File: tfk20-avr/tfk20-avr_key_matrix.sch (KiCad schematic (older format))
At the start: 48 parts

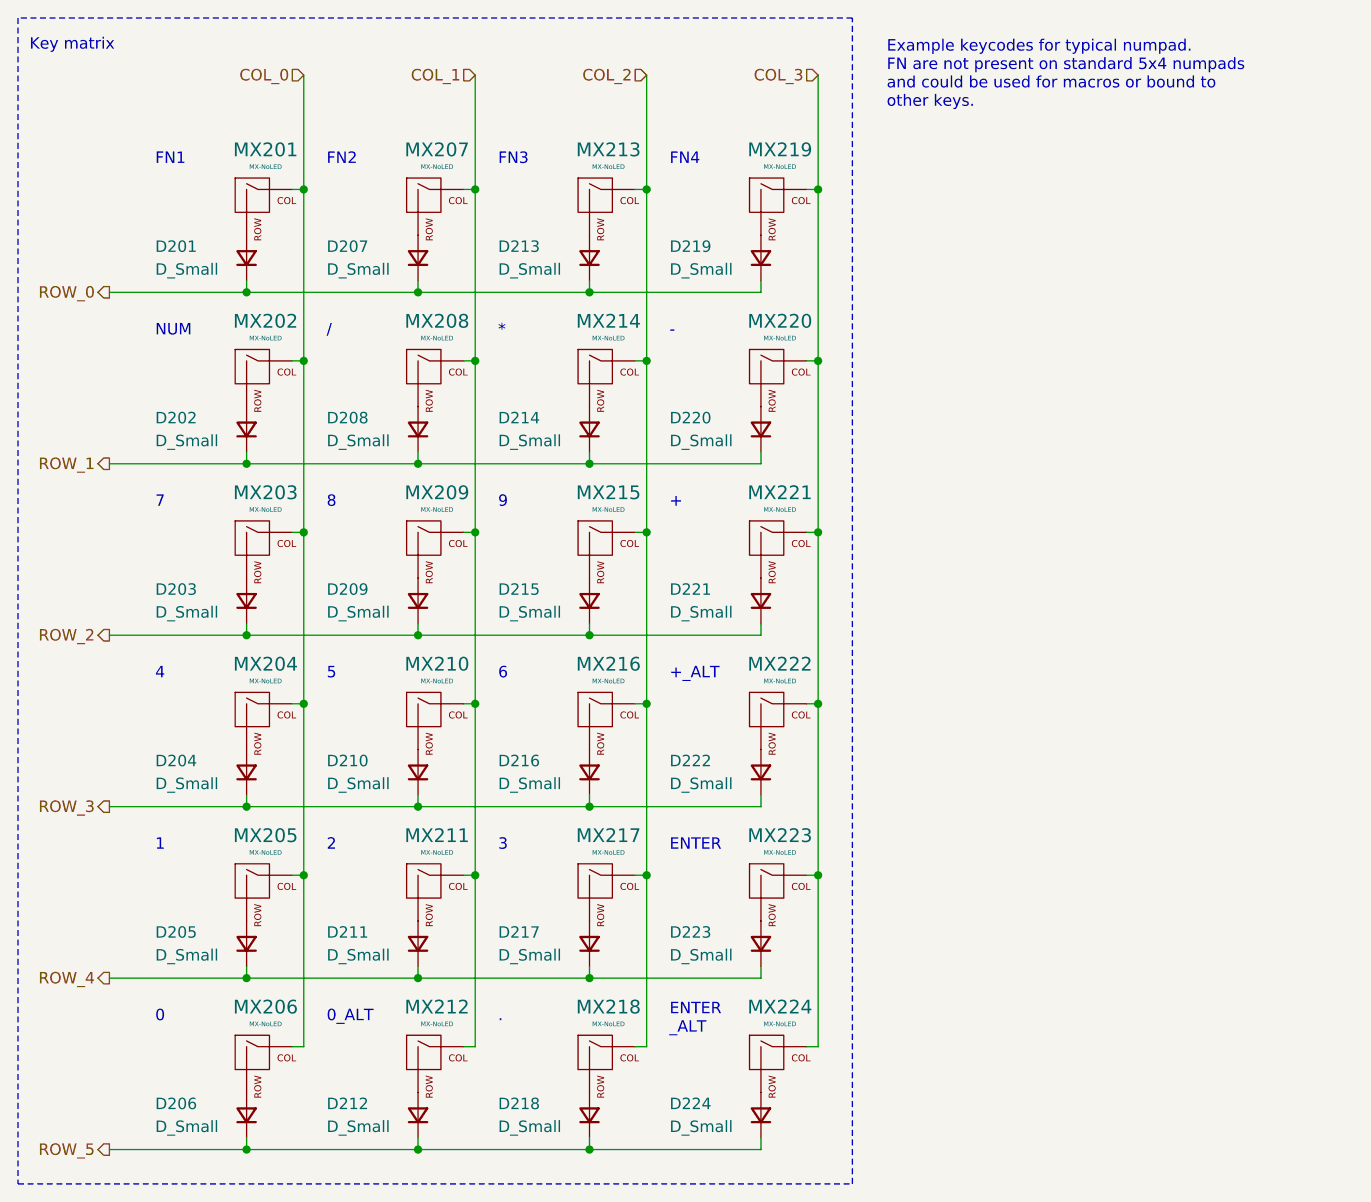
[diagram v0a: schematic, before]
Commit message: Add mounting holes
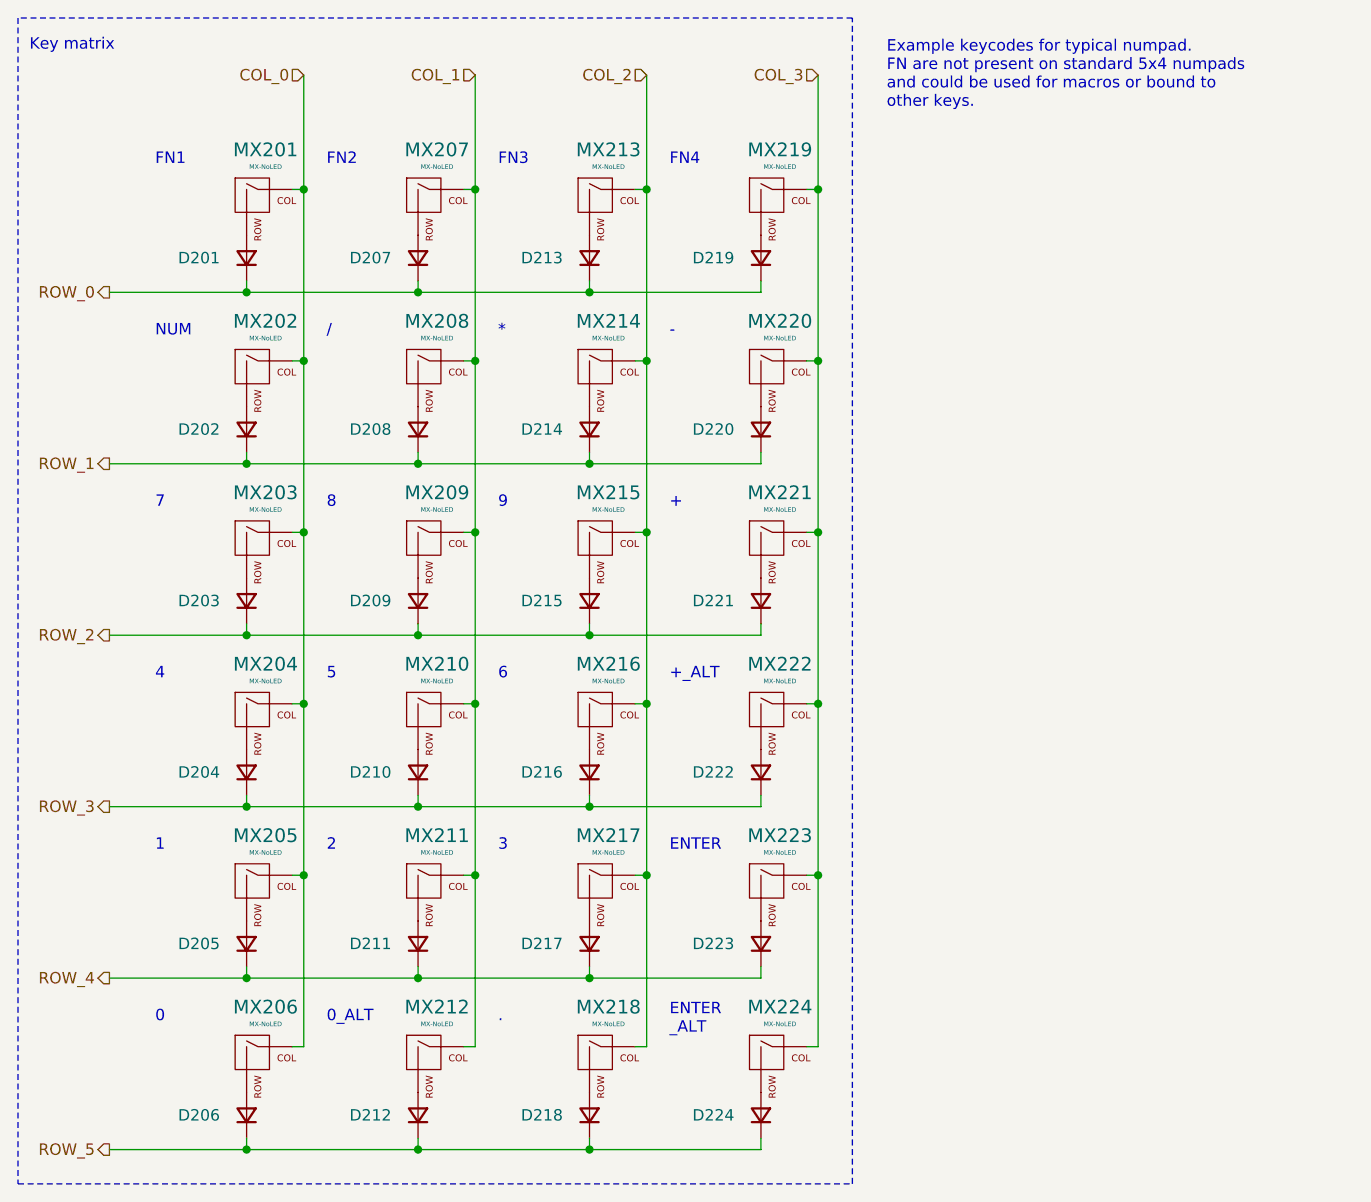
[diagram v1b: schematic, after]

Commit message: Remove alternative switch positions
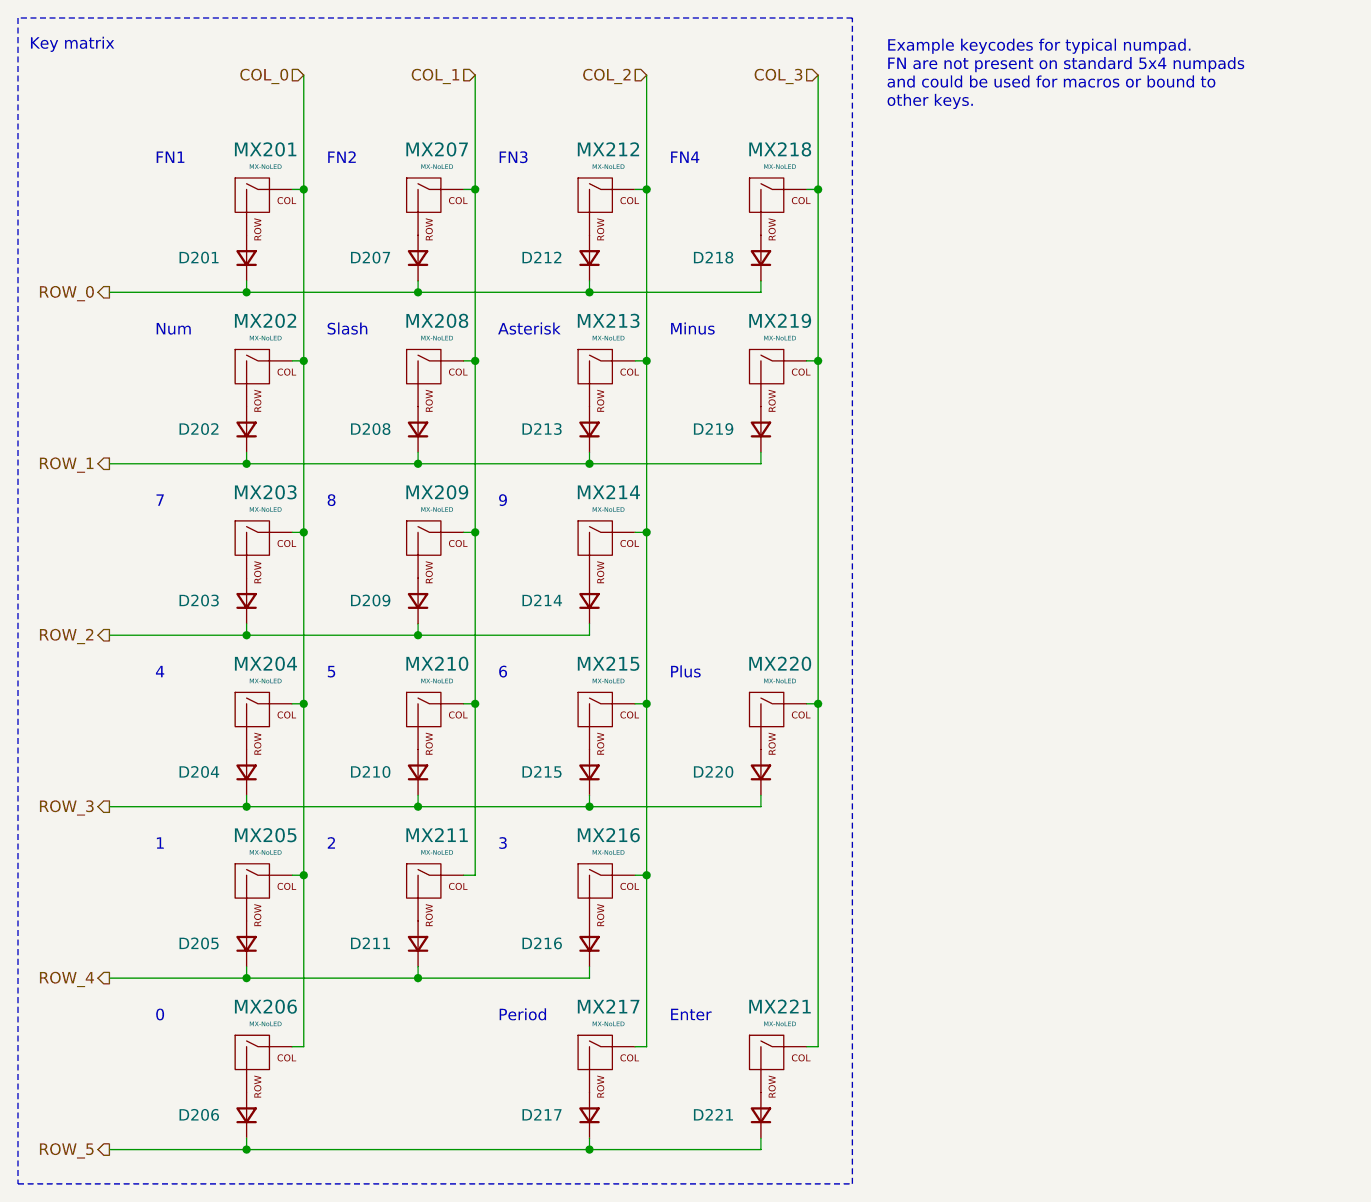
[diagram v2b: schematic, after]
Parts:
- removed D212, D221, D223: D_Small, symbol Device:D_Small
- removed MX212, MX221, MX223: MX-NoLED, symbol MX_Alps_Hybrid:MX-NoLED
- renumbered D213 to D212, D214 to D213, D215 to D214, D216 to D215, D217 to D216, D218 to D217, D219 to D218, D220 to D219, D222 to D220, D224 to D221, MX213 to MX212, MX214 to MX213, MX215 to MX214, MX216 to MX215, MX217 to MX216, MX218 to MX217, MX219 to MX218, MX220 to MX219, MX222 to MX220, MX224 to MX221
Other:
- note added: "Asterisk"
- note added: "Enter"
- note added: "Minus"
- note added: "Num"
- note added: "Period"
- note added: "Plus"
- note added: "Slash"
- note removed: "*"
- note removed: "+"
- note removed: "+_ALT"
- note removed: "-"
- note removed: "."
- note removed: "/"
- note removed: "0_ALT"
- note removed: "ENTER"
- note removed: "ENTER\n_ALT"
- note removed: "NUM\n"
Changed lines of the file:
@@
 $EndComp
 $Comp
-L MX_Alps_Hybrid:MX-NoLED MX214
+L MX_Alps_Hybrid:MX-NoLED MX213
 U 1 1 60307FEB
 P 6150 2550
-F 0 "MX214" H 6183 2773 60  0000 C CNN
+F 0 "MX213" H 6183 2773 60  0000 C CNN
 F 1 "MX-NoLED" H 6183 2699 20  0000 C CNN
 F 2 "" H 5525 2525 60  0001 C CNN
@@
 $EndComp
 $Comp
-L MX_Alps_Hybrid:MX-NoLED MX215
+L MX_Alps_Hybrid:MX-NoLED MX214
 U 1 1 60307FF7
 P 6150 3300
-F 0 "MX215" H 6183 3523 60  0000 C CNN
+F 0 "MX214" H 6183 3523 60  0000 C CNN
 F 1 "MX-NoLED" H 6183 3449 20  0000 C CNN
 F 2 "" H 5525 3275 60  0001 C CNN
@@
 $EndComp
 $Comp
-L MX_Alps_Hybrid:MX-NoLED MX220
+L MX_Alps_Hybrid:MX-NoLED MX219
 U 1 1 60307FFD
 P 6900 2550
-F 0 "MX220" H 6933 2773 60  0000 C CNN
+F 0 "MX219" H 6933 2773 60  0000 C CNN
 F 1 "MX-NoLED" H 6933 2699 20  0000 C CNN
 F 2 "" H 6275 2525 60  0001 C CNN
 F 3 "" H 6275 2525 60  0001 C CNN
 	1    6900 2550
-	1    0    0    -1
-$EndComp
-$Comp
-L MX_Alps_Hybrid:MX-NoLED MX221
-U 1 1 60308003
-P 6900 3300
-F 0 "MX221" H 6933 3523 60  0000 C CNN
-F 1 "MX-NoLED" H 6933 3449 20  0000 C CNN
-F 2 "" H 6275 3275 60  0001 C CNN
-F 3 "" H 6275 3275 60  0001 C CNN
-	1    6900 3300
 	1    0    0    -1
 $EndComp
@@
 $EndComp
 $Comp
-L MX_Alps_Hybrid:MX-NoLED MX216
+L MX_Alps_Hybrid:MX-NoLED MX215
 U 1 1 60314CE4
 P 6150 4050
-F 0 "MX216" H 6183 4273 60  0000 C CNN
+F 0 "MX215" H 6183 4273 60  0000 C CNN
 F 1 "MX-NoLED" H 6183 4199 20  0000 C CNN
 F 2 "" H 5525 4025 60  0001 C CNN
@@
 $EndComp
 $Comp
-L MX_Alps_Hybrid:MX-NoLED MX222
+L MX_Alps_Hybrid:MX-NoLED MX220
 U 1 1 60314CEA
 P 6900 4050
-F 0 "MX222" H 6933 4273 60  0000 C CNN
+F 0 "MX220" H 6933 4273 60  0000 C CNN
 F 1 "MX-NoLED" H 6933 4199 20  0000 C CNN
 F 2 "" H 6275 4025 60  0001 C CNN
@@
 $EndComp
 $Comp
-L MX_Alps_Hybrid:MX-NoLED MX217
+L MX_Alps_Hybrid:MX-NoLED MX216
 U 1 1 6031D490
 P 6150 4800
-F 0 "MX217" H 6183 5023 60  0000 C CNN
+F 0 "MX216" H 6183 5023 60  0000 C CNN
 F 1 "MX-NoLED" H 6183 4949 20  0000 C CNN
 F 2 "" H 5525 4775 60  0001 C CNN
 F 3 "" H 5525 4775 60  0001 C CNN
 	1    6150 4800
-	1    0    0    -1
-$EndComp
-$Comp
-L MX_Alps_Hybrid:MX-NoLED MX223
-U 1 1 6031D496
-P 6900 4800
-F 0 "MX223" H 6933 5023 60  0000 C CNN
-F 1 "MX-NoLED" H 6933 4949 20  0000 C CNN
-F 2 "" H 6275 4775 60  0001 C CNN
-F 3 "" H 6275 4775 60  0001 C CNN
-	1    6900 4800
 	1    0    0    -1
 $EndComp
@@
 $EndComp
 $Comp
-L MX_Alps_Hybrid:MX-NoLED MX212
-U 1 1 6032525B
-P 5400 5550
-F 0 "MX212" H 5433 5773 60  0000 C CNN
-F 1 "MX-NoLED" H 5433 5699 20  0000 C CNN
-F 2 "" H 4775 5525 60  0001 C CNN
-F 3 "" H 4775 5525 60  0001 C CNN
-	1    5400 5550
-	1    0    0    -1
-$EndComp
-$Comp
-L MX_Alps_Hybrid:MX-NoLED MX218
+L MX_Alps_Hybrid:MX-NoLED MX217
 U 1 1 6032526D
 P 6150 5550
-F 0 "MX218" H 6183 5773 60  0000 C CNN
+F 0 "MX217" H 6183 5773 60  0000 C CNN
 F 1 "MX-NoLED" H 6183 5699 20  0000 C CNN
 F 2 "" H 5525 5525 60  0001 C CNN
@@
 $EndComp
 $Comp
-L MX_Alps_Hybrid:MX-NoLED MX224
+L MX_Alps_Hybrid:MX-NoLED MX221
 U 1 1 60325273
 P 6900 5550
-F 0 "MX224" H 6933 5773 60  0000 C CNN
+F 0 "MX221" H 6933 5773 60  0000 C CNN
 F 1 "MX-NoLED" H 6933 5699 20  0000 C CNN
 F 2 "" H 6275 5525 60  0001 C CNN
@@
 	4850 5500 4800 5500
 Wire Wire Line
-	5600 5500 5550 5500
-Wire Wire Line
 	6350 5500 6300 5500
 Wire Wire Line
@@
 Wire Wire Line
 	5550 4750 5600 4750
-Connection ~ 5600 4750
-Wire Wire Line
-	5600 4750 5600 5500
 Wire Wire Line
 	6300 2500 6350 2500
@@
 	6350 4750 6350 5500
 Wire Wire Line
-	7050 4750 7100 4750
-Connection ~ 7100 4750
-Wire Wire Line
-	7100 4750 7100 5500
-Wire Wire Line
 	7050 4000 7100 4000
 Connection ~ 7100 4000
 Wire Wire Line
-	7100 4000 7100 4750
-Wire Wire Line
-	7050 3250 7100 3250
-Connection ~ 7100 3250
-Wire Wire Line
-	7100 3250 7100 4000
-Wire Wire Line
 	7050 2500 7100 2500
 Connection ~ 7100 2500
@@
 	4000 3700 4600 3700
 Wire Wire Line
-	6850 3700 6850 3650
-Wire Wire Line
 	6100 3650 6100 3700
-Connection ~ 6100 3700
-Wire Wire Line
-	6100 3700 6850 3700
 Wire Wire Line
 	5350 3650 5350 3700
@@
 	4000 5200 4600 5200
 Wire Wire Line
-	6850 5200 6850 5150
-Wire Wire Line
 	6100 5150 6100 5200
-Connection ~ 6100 5200
-Wire Wire Line
-	6100 5200 6850 5200
 Wire Wire Line
 	5350 5150 5350 5200
@@
 Wire Wire Line
 	4600 5950 4600 5900
-Wire Wire Line
-	4600 5950 5350 5950
-Wire Wire Line
-	5350 5950 5350 5900
 Connection ~ 4600 5950
 Wire Wire Line
-	5350 5950 6100 5950
-Wire Wire Line
 	6100 5950 6100 5900
-Connection ~ 5350 5950
 Wire Wire Line
 	6850 5900 6850 5950
@@
 Connection ~ 6100 5950
 Text Notes 4200 2400 0    50   ~ 0
-NUM\n
+Num
 Text Notes 4950 2400 0    50   ~ 0
-/
+Slash
 Text Notes 5700 2400 0    50   ~ 0
-*
+Asterisk
 Text Notes 6450 2400 0    50   ~ 0
--
+Minus
 Text Notes 4200 3150 0    50   ~ 0
 7
@@
 0
 Text Notes 5700 5400 0    50   ~ 0
-.
-Text Notes 4950 5400 0    50   ~ 0
-0_ALT
-Text Notes 6450 3150 0    50   ~ 0
-+
+Period
 Text Notes 6450 3900 0    50   ~ 0
-+_ALT
-Text Notes 6450 4650 0    50   ~ 0
-ENTER
-Text Notes 6450 5450 0    50   ~ 0
-ENTER\n_ALT
+Plus
+Text Notes 6450 5400 0    50   ~ 0
+Enter
 Text Notes 3650 1150 0    50   ~ 0
 Key matrix
@@
 $EndComp
 $Comp
-L MX_Alps_Hybrid:MX-NoLED MX213
+L MX_Alps_Hybrid:MX-NoLED MX212
 U 1 1 60A22945
 P 6150 1800
-F 0 "MX213" H 6183 2023 60  0000 C CNN
+F 0 "MX212" H 6183 2023 60  0000 C CNN
 F 1 "MX-NoLED" H 6183 1949 20  0000 C CNN
 F 2 "" H 5525 1775 60  0001 C CNN
@@
 $EndComp
 $Comp
-L MX_Alps_Hybrid:MX-NoLED MX219
+L MX_Alps_Hybrid:MX-NoLED MX218
 U 1 1 60A2294B
 P 6900 1800
-F 0 "MX219" H 6933 2023 60  0000 C CNN
+F 0 "MX218" H 6933 2023 60  0000 C CNN
 F 1 "MX-NoLED" H 6933 1949 20  0000 C CNN
 F 2 "" H 6275 1775 60  0001 C CNN
@@
 Text HLabel 4000 5950 0    50   Output ~ 0
 ROW_5
-Wire Wire Line
-	7100 2500 7100 3250
 Wire Wire Line
 	6350 1750 6350 2500
@@
 $EndComp
 $Comp
-L Device:D_Small D213
+L Device:D_Small D212
 U 1 1 60BB2F94
 P 6100 2050
-F 0 "D213" V 6100 2350 50  0000 R CNN
+F 0 "D212" V 6100 2350 50  0000 R CNN
 F 1 "D_Small" V 6050 2450 50  0001 R CNN
 F 2 "" V 6100 2050 50  0001 C CNN
@@
 $EndComp
 $Comp
-L Device:D_Small D219
+L Device:D_Small D218
 U 1 1 60BB37C1
 P 6850 2050
-F 0 "D219" V 6850 2350 50  0000 R CNN
+F 0 "D218" V 6850 2350 50  0000 R CNN
 F 1 "D_Small" V 6800 2450 50  0001 R CNN
 F 2 "" V 6850 2050 50  0001 C CNN
@@
 $EndComp
 $Comp
-L Device:D_Small D214
+L Device:D_Small D213
 U 1 1 60BB50B6
 P 6100 2800
-F 0 "D214" V 6100 3100 50  0000 R CNN
+F 0 "D213" V 6100 3100 50  0000 R CNN
 F 1 "D_Small" V 6050 3200 50  0001 R CNN
 F 2 "" V 6100 2800 50  0001 C CNN
@@
 $EndComp
 $Comp
-L Device:D_Small D220
+L Device:D_Small D219
 U 1 1 60BB580C
 P 6850 2800
-F 0 "D220" V 6850 3100 50  0000 R CNN
+F 0 "D219" V 6850 3100 50  0000 R CNN
 F 1 "D_Small" V 6800 3200 50  0001 R CNN
 F 2 "" V 6850 2800 50  0001 C CNN
@@
 $EndComp
 $Comp
-L Device:D_Small D215
+L Device:D_Small D214
 U 1 1 60BB6E36
 P 6100 3550
-F 0 "D215" V 6100 3850 50  0000 R CNN
+F 0 "D214" V 6100 3850 50  0000 R CNN
 F 1 "D_Small" V 6050 3950 50  0001 R CNN
 F 2 "" V 6100 3550 50  0001 C CNN
 F 3 "~" V 6100 3550 50  0001 C CNN
 	1    6100 3550
-	0    -1   -1   0
-$EndComp
-$Comp
-L Device:D_Small D221
-U 1 1 60BB7686
-P 6850 3550
-F 0 "D221" V 6850 3850 50  0000 R CNN
-F 1 "D_Small" V 6800 3950 50  0001 R CNN
-F 2 "" V 6850 3550 50  0001 C CNN
-F 3 "~" V 6850 3550 50  0001 C CNN
-	1    6850 3550
 	0    -1   -1   0
 $EndComp
@@
 $EndComp
 $Comp
-L Device:D_Small D216
+L Device:D_Small D215
 U 1 1 60BB89C7
 P 6100 4300
-F 0 "D216" V 6100 4600 50  0000 R CNN
+F 0 "D215" V 6100 4600 50  0000 R CNN
 F 1 "D_Small" V 6050 4700 50  0001 R CNN
 F 2 "" V 6100 4300 50  0001 C CNN
@@
 $EndComp
 $Comp
-L Device:D_Small D222
+L Device:D_Small D220
 U 1 1 60BB918B
 P 6850 4300
-F 0 "D222" V 6850 4600 50  0000 R CNN
+F 0 "D220" V 6850 4600 50  0000 R CNN
 F 1 "D_Small" V 6800 4700 50  0001 R CNN
 F 2 "" V 6850 4300 50  0001 C CNN
@@
 $EndComp
 $Comp
-L Device:D_Small D217
+L Device:D_Small D216
 U 1 1 60BBA9EF
 P 6100 5050
-F 0 "D217" V 6100 5350 50  0000 R CNN
+F 0 "D216" V 6100 5350 50  0000 R CNN
 F 1 "D_Small" V 6050 5450 50  0001 R CNN
 F 2 "" V 6100 5050 50  0001 C CNN
 F 3 "~" V 6100 5050 50  0001 C CNN
 	1    6100 5050
-	0    -1   -1   0
-$EndComp
-$Comp
-L Device:D_Small D223
-U 1 1 60BBB19A
-P 6850 5050
-F 0 "D223" V 6850 5350 50  0000 R CNN
-F 1 "D_Small" V 6800 5450 50  0001 R CNN
-F 2 "" V 6850 5050 50  0001 C CNN
-F 3 "~" V 6850 5050 50  0001 C CNN
-	1    6850 5050
 	0    -1   -1   0
 $EndComp
@@
 $EndComp
 $Comp
-L Device:D_Small D212
-U 1 1 60BBBF47
-P 5350 5800
-F 0 "D212" V 5350 6100 50  0000 R CNN
-F 1 "D_Small" V 5300 6200 50  0001 R CNN
-F 2 "" V 5350 5800 50  0001 C CNN
-F 3 "~" V 5350 5800 50  0001 C CNN
-	1    5350 5800
-	0    -1   -1   0
-$EndComp
-$Comp
-L Device:D_Small D218
+L Device:D_Small D217
 U 1 1 60BBC88C
 P 6100 5800
-F 0 "D218" V 6100 6100 50  0000 R CNN
+F 0 "D217" V 6100 6100 50  0000 R CNN
 F 1 "D_Small" V 6050 6200 50  0001 R CNN
 F 2 "" V 6100 5800 50  0001 C CNN
@@
 $EndComp
 $Comp
-L Device:D_Small D224
+L Device:D_Small D221
 U 1 1 60BBCFA6
 P 6850 5800
-F 0 "D224" V 6850 6100 50  0000 R CNN
+F 0 "D221" V 6850 6100 50  0000 R CNN
 F 1 "D_Small" V 6800 6200 50  0001 R CNN
 F 2 "" V 6850 5800 50  0001 C CNN
@@
 	0    -1   -1   0
 $EndComp
+Wire Wire Line
+	7100 2500 7100 4000
+Wire Wire Line
+	7100 4000 7100 5500
+Wire Wire Line
+	4600 5950 6100 5950
 $EndSCHEMATC
